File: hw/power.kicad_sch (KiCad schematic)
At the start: 53 parts, among them Q1 BSS138PW,115, U2 MUN3CAD01-SC, U3 MUN3CAD01-SC, U4 MUN3CAD01-SC, U5 AP3012, U6 LT3042xMSE

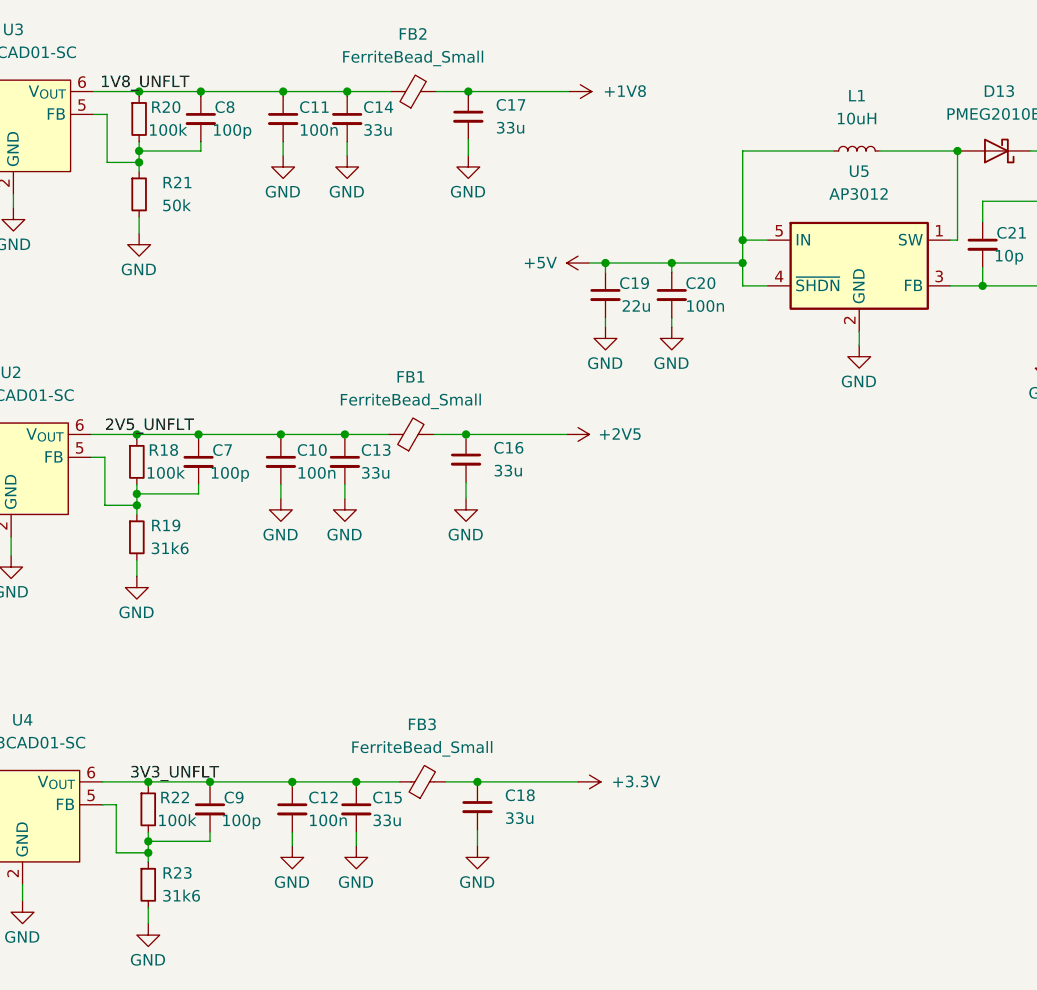
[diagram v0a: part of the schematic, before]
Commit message: schematic fixes and adding sw section
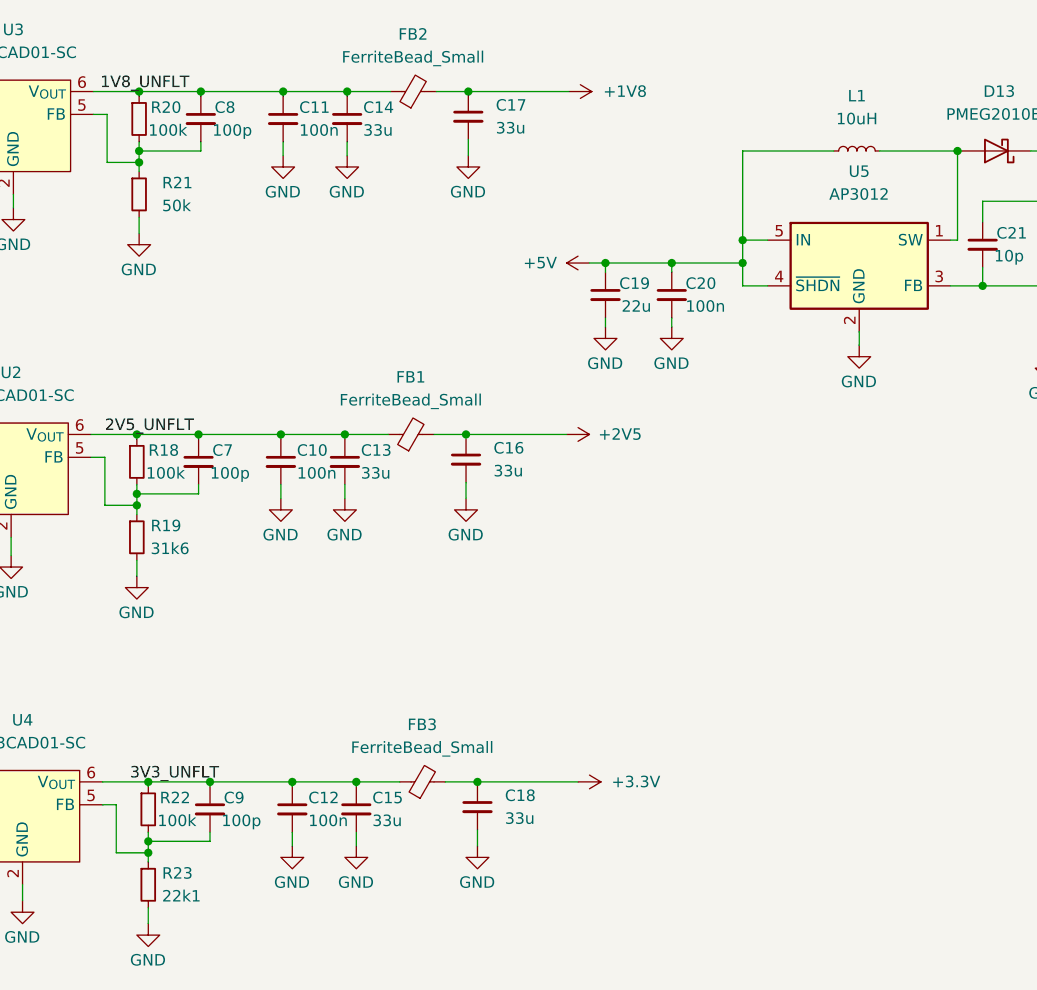
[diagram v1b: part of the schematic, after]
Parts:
- R23: value 31k6 -> 22k1
